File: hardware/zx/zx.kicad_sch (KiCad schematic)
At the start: 42 parts, among them J1 ZX Keyboard, J10 Conn_01x01, J11 Conn_01x01, J12 Conn_01x01, J13 Conn_01x01, J14 Conn_01x01, J15 Conn_01x01, J16 Conn_01x01, J17 Conn_01x01, J18 Conn_01x01, J19 Conn_01x01, J2 GOTEK, J20 Conn_01x01, J21 Conn_01x01, J22 Conn_01x01, J3 UART, J4 USB_A, J5 USB_A, J6 Keyboard, J7 Mouse, J8 Kempston Mouse, J9 Z80, SW1 RESET, SW2 BOOT0, SW3 BOOT1, U1 CH559L, U2 CH446Q, Y1 12MHz

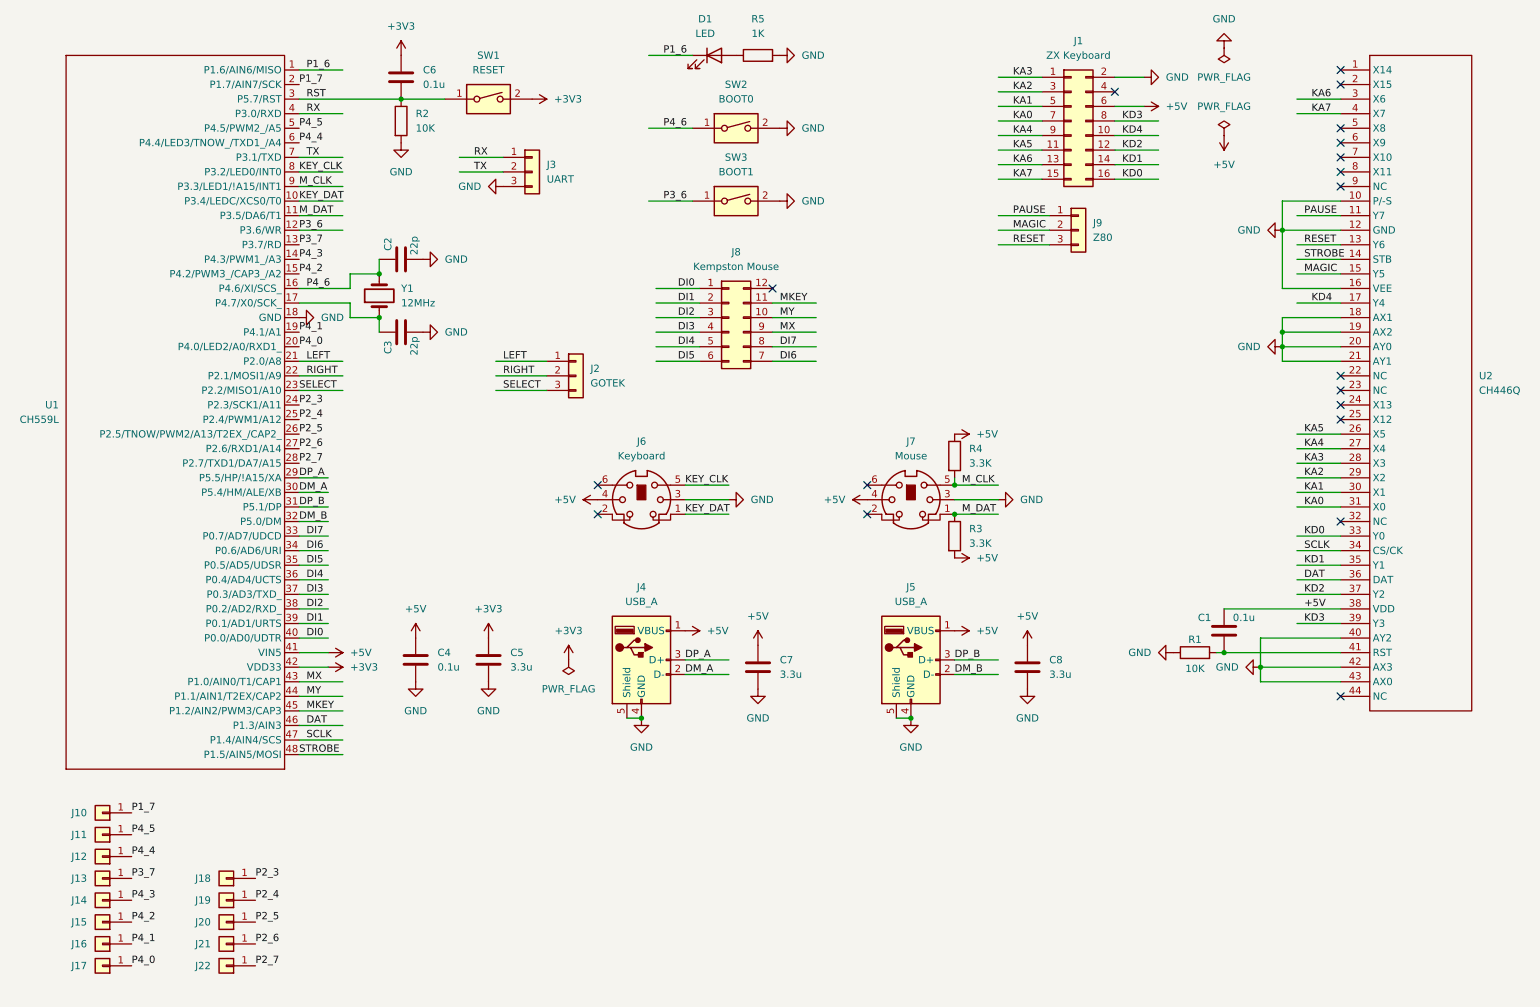
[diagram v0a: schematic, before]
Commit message: Initial PCB layout.
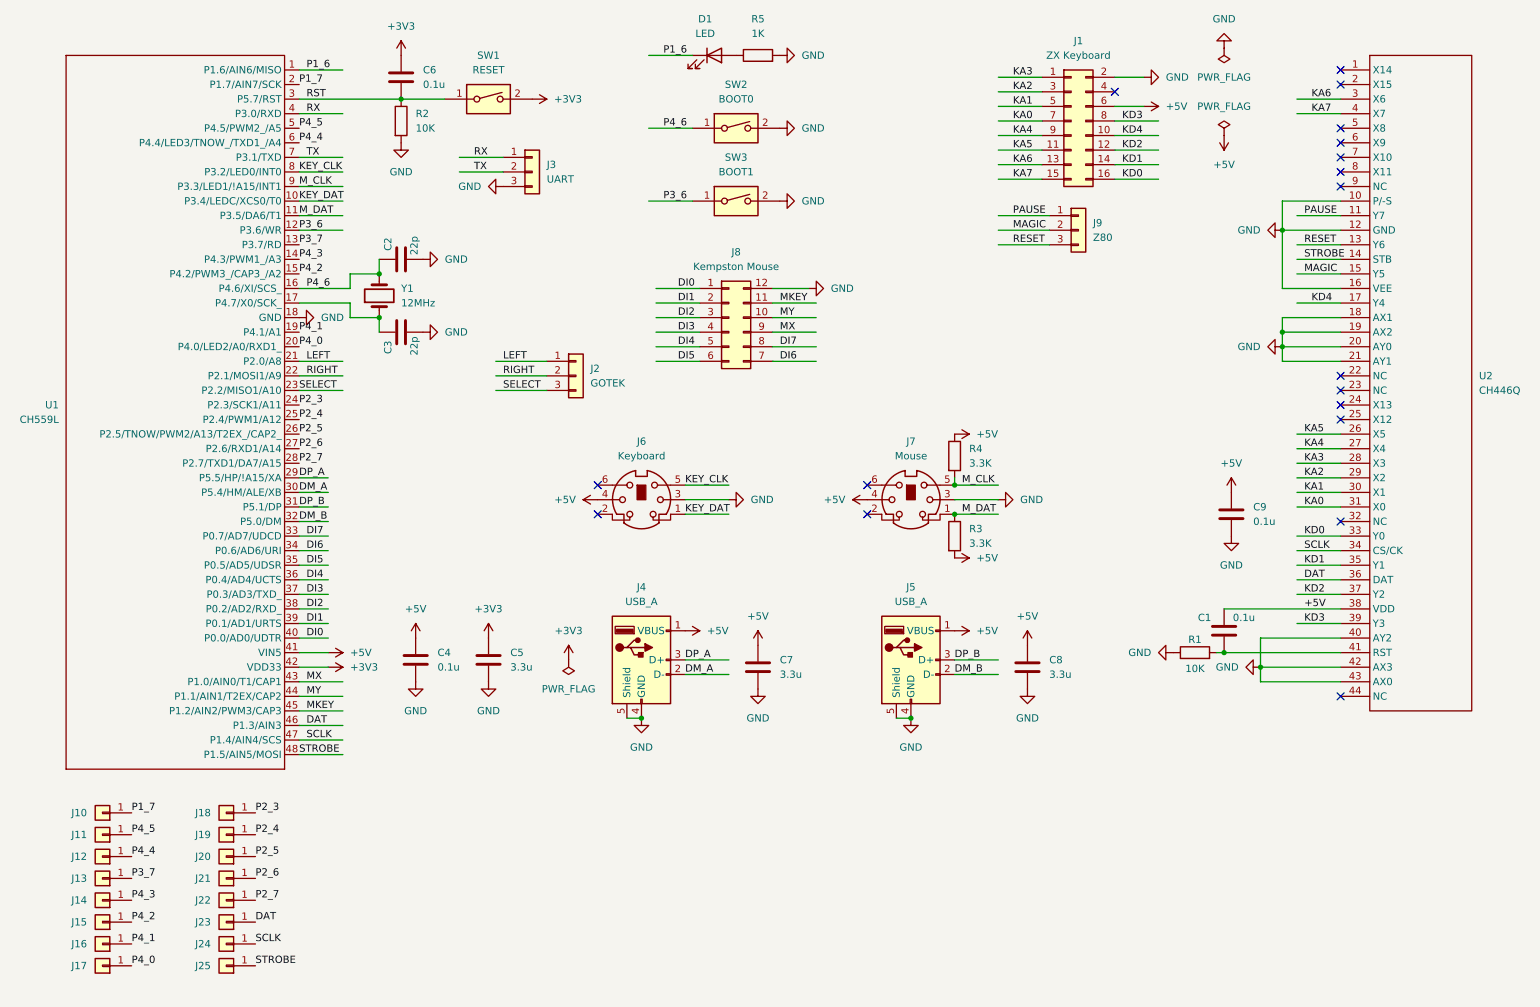
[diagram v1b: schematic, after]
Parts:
- added C9: 0.1u, Capacitor_SMD:C_1206_3216Metric_Pad1.33x1.80mm_HandSolder, symbol Device:C
- added J23, J24, J25: Conn_01x01, THT_Pin:THT_Pin_Vertical, symbol Connector_Generic:Conn_01x01
- J10, J11, J12, J13, J14, J15, J16, J17, J18, J19, J20, J21, J22: footprint Connector_PinHeader_2.54mm:PinHeader_1x01_P2.54mm_Vertical -> THT_Pin:THT_Pin_Vertical
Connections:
- net +5V: now also C9.1
- net DAT: now also J23.1 (Pin_1)
- net GND: now also J8.12 (Pin_12), C9.2
- net SCLK: now also J24.1 (Pin_1)
- net STROBE: now also J25.1 (Pin_1)
- no-connect marks 19 -> 18
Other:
- moved on the sheet: J18, J19, J20, J21, J22

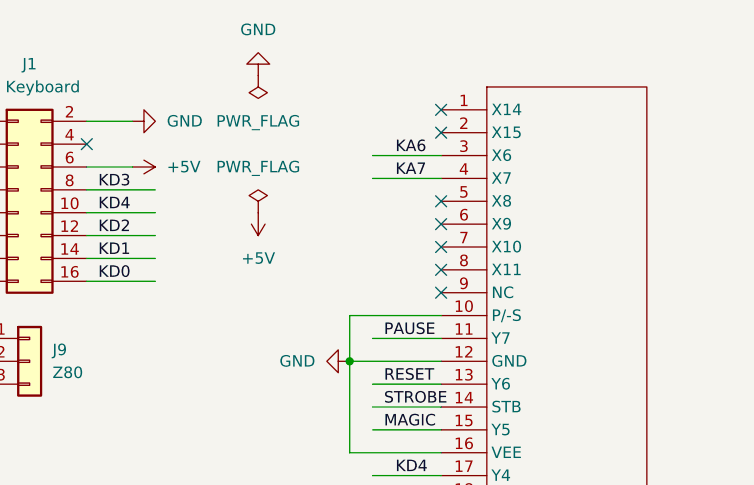
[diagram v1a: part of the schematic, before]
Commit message: CH446Q output Z80 control signals PAUSE, MAGIC, RESET have common input connected to GND.
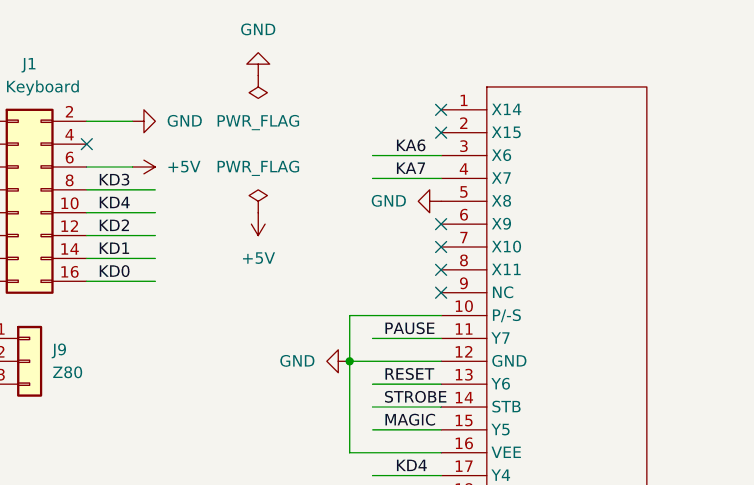
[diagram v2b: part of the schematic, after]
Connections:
- net GND: now also U2.5 (X8)
- no-connect marks 18 -> 17
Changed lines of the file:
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@@
 	)
 	(no_connect
-		(at 247.65 34.29)
-	)
-	(no_connect
 		(at 247.65 24.13)
 	)
@@
 					(unit 1)
 				)
+			)
+		)
+	)
+	(symbol
+		(lib_id "power:GND")
+		(at 247.65 34.29 270)
+		(unit 1)
+		(exclude_from_sim no)
+		(in_bom yes)
+		(on_board yes)
+		(dnp no)
+		(fields_autoplaced yes)
+		(property "Reference" "#PWR043"
+			(at 241.3 34.29 0)
+			(effects
+				(font
+					(size 1.27 1.27)
+				)
+				(hide yes)
+			)
+		)
+		(property "Value" "GND"
+			(at 243.84 34.2899 90)
+			(effects
+				(font
+					(size 1.27 1.27)
+				)
+				(justify right)
+			)
+		)
+		(property "Footprint" ""
+			(at 247.65 34.29 0)
+			(effects
+				(font
+					(size 1.27 1.27)
+				)
+				(hide yes)
+			)
+		)
+		(property "Datasheet" ""
+			(at 247.65 34.29 0)
+			(effects
+				(font
+					(size 1.27 1.27)
+				)
+				(hide yes)
+			)
+		)
+		(property "Description" "Power symbol creates a global label with name \"GND\" , ground"
+			(at 247.65 34.29 0)
+			(effects
+				(font
+					(size 1.27 1.27)
+				)
+				(hide yes)
+			)
+		)
+		(pin "1"
+		)
+		(instances
+			(project "zx"
+				(path "/e686a5db-35f9-40ca-bbb5-69eb58ec1522"
+					(reference "#PWR043")
+					(unit 1)
+				)

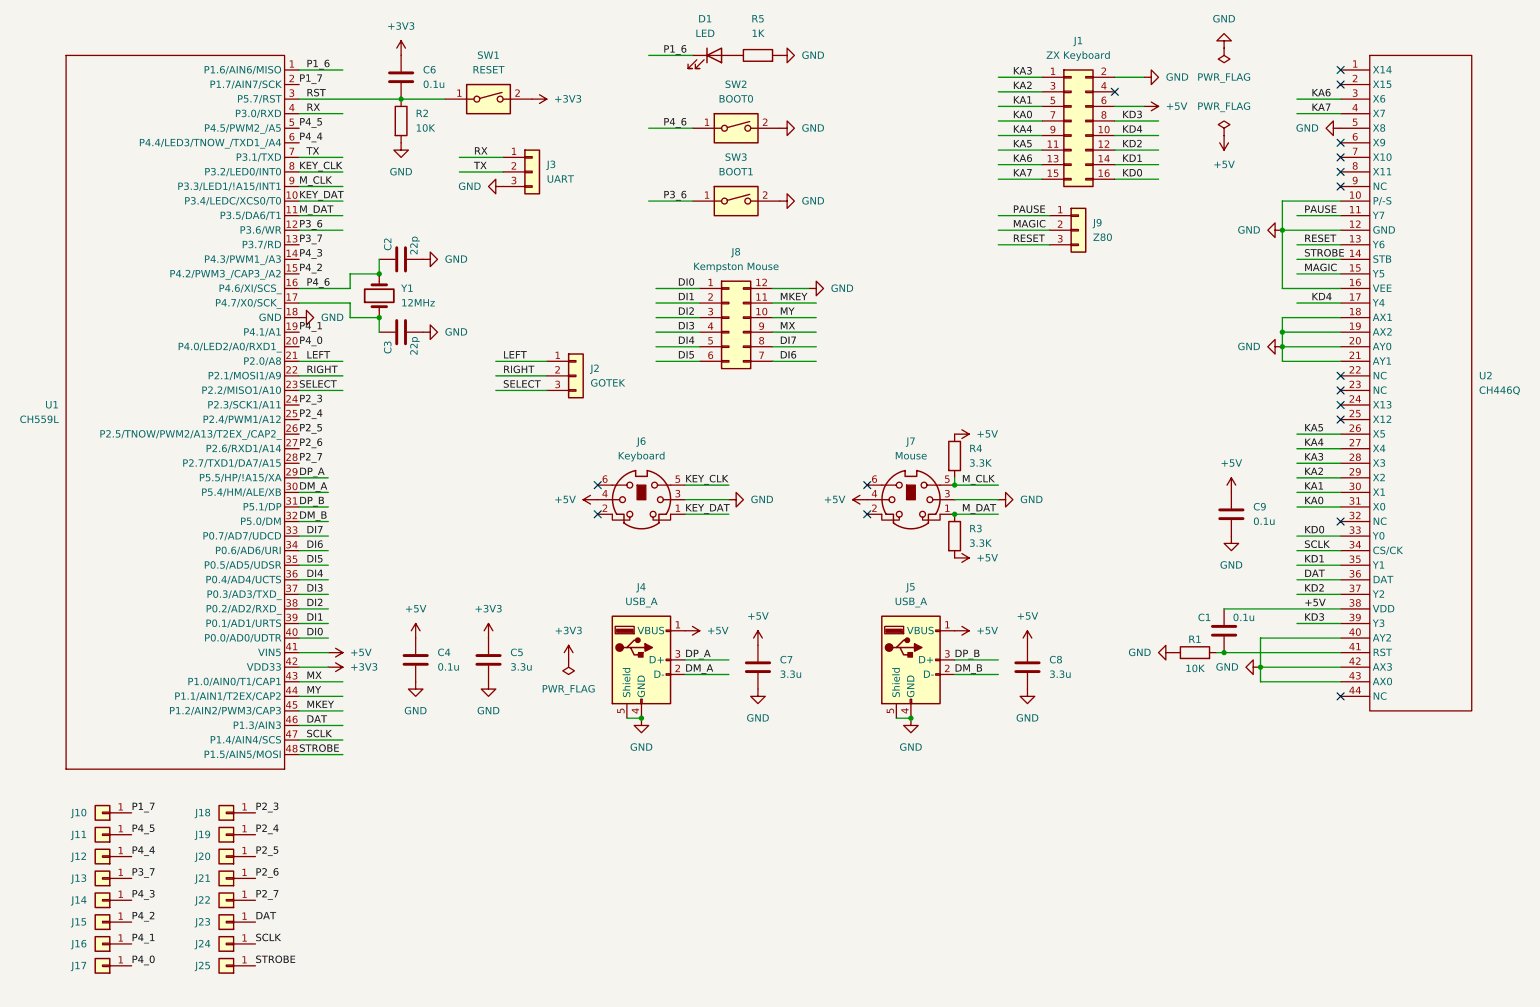
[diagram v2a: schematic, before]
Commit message: Reserve P1.6 for Kempston Joystick DI write strobe (JOY). Move activity LED to P1.7. Add free-standing GND pin. Add J8 GND label.
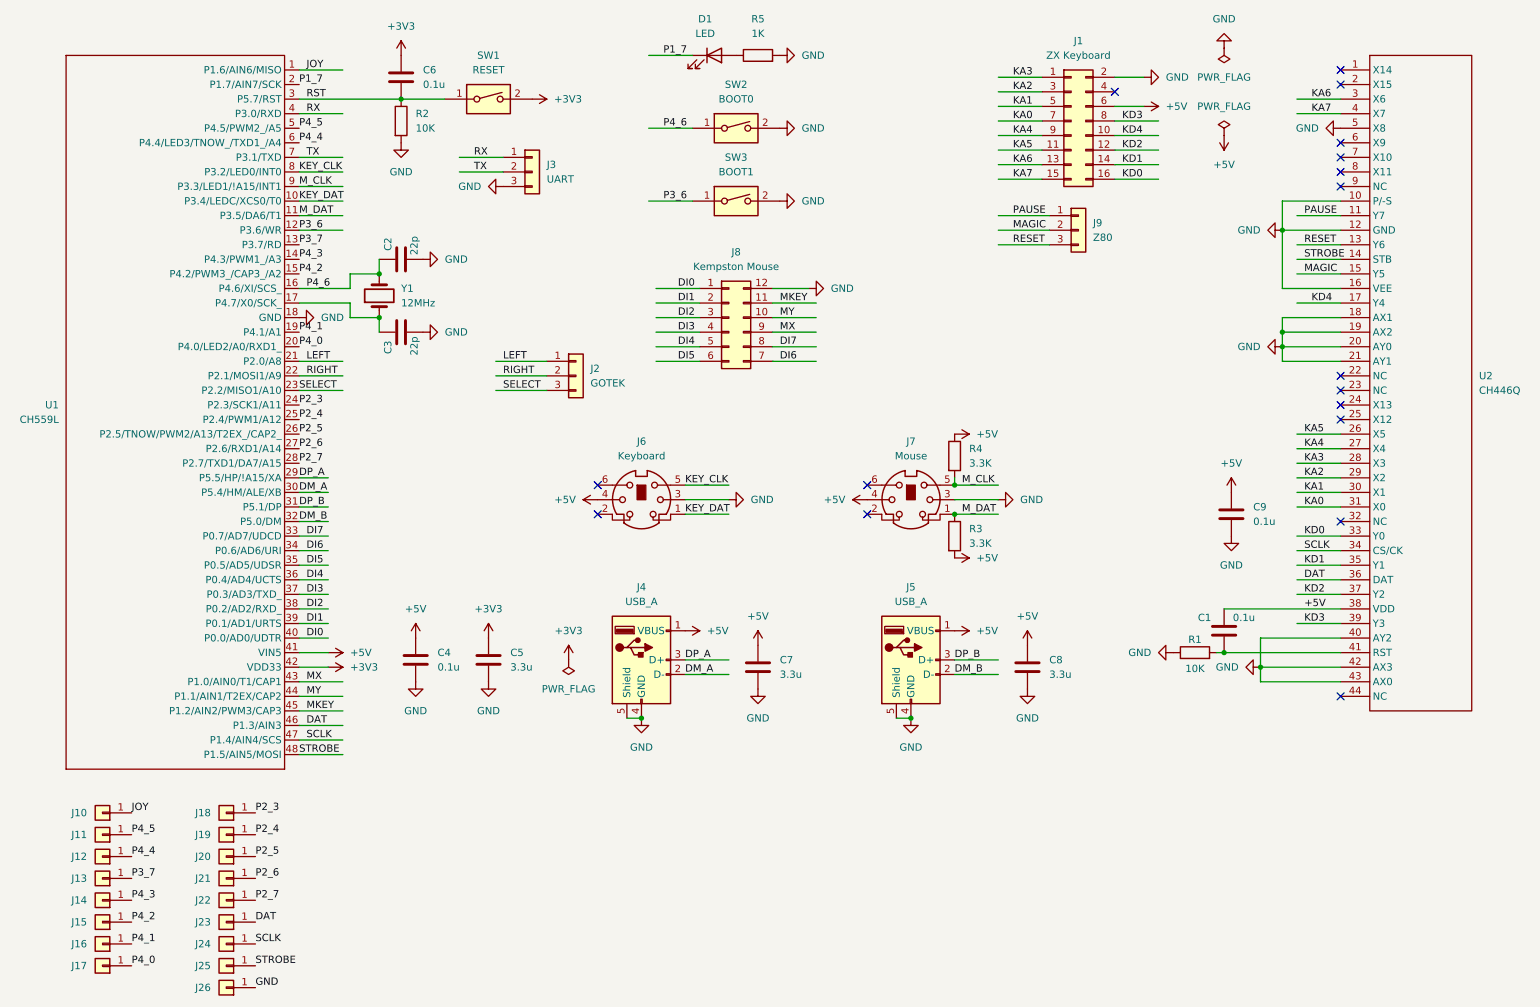
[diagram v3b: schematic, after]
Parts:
- added J26: Conn_01x01, THT_Pin:THT_Pin_Vertical, symbol Connector_Generic:Conn_01x01
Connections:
- net GND: now also J26.1 (Pin_1)
- net P1_7: now also D1.1 (K); no longer J10.1 (Pin_1)
- net P1_6 renamed JOY
- net JOY: now also J10.1 (Pin_1); no longer D1.1 (K)
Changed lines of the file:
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@@
 		)
 	)
-	(label "P1_6"
+	(label "P1_7"
 		(at 129.54 21.59 0)
 		(fields_autoplaced yes)
@@
 		)
 	)
-	(label "P1_7"
+	(label "JOY"
 		(at 36.83 153.67 0)
 		(fields_autoplaced yes)
@@
 		)
 	)
+	(label "GND"
+		(at 58.42 184.15 0)
+		(fields_autoplaced yes)
+		(effects
+			(font
+				(size 1.27 1.27)
+			)
+			(justify left bottom)
+		)
+	)
 	(label "PAUSE"
 		(at 241.3 49.53 0)
@@
 		)
 	)
-	(label "P1_6"
+	(label "JOY"
 		(at 67.31 24.13 0)
 		(fields_autoplaced yes)
@@
 					(unit 1)
 				)
+			)
+		)
+	)
+	(symbol
+		(lib_id "Connector_Generic:Conn_01x01")
+		(at 53.34 184.15 180)
+		(unit 1)
+		(exclude_from_sim no)
+		(in_bom yes)
+		(on_board yes)
+		(dnp no)
+		(property "Reference" "J26"
+			(at 49.276 184.15 0)
+			(effects
+				(font
+					(size 1.27 1.27)
+				)
+			)
+		)
+		(property "Value" "Conn_01x01"
+			(at 53.34 180.34 0)
+			(effects
+				(font
+					(size 1.27 1.27)
+				)
+				(hide yes)
+			)
+		)
+		(property "Footprint" "THT_Pin:THT_Pin_Vertical"
+			(at 53.34 184.15 0)
+			(effects
+				(font
+					(size 1.27 1.27)
+				)
+				(hide yes)
+			)
+		)
+		(property "Datasheet" "~"
+			(at 53.34 184.15 0)
+			(effects
+				(font
+					(size 1.27 1.27)
+				)
+				(hide yes)
+			)
+		)
+		(property "Description" "Generic connector, single row, 01x01, script generated (kicad-library-utils/schlib/autogen/connector/)"
+			(at 53.34 184.15 0)
+			(effects
+				(font
+					(size 1.27 1.27)
+				)
+				(hide yes)
+			)
+		)
+		(pin "1"
+		)
+		(instances
+			(project "zx"
+				(path "/e686a5db-35f9-40ca-bbb5-69eb58ec1522"
+					(reference "J26")
+					(unit 1)
+				)

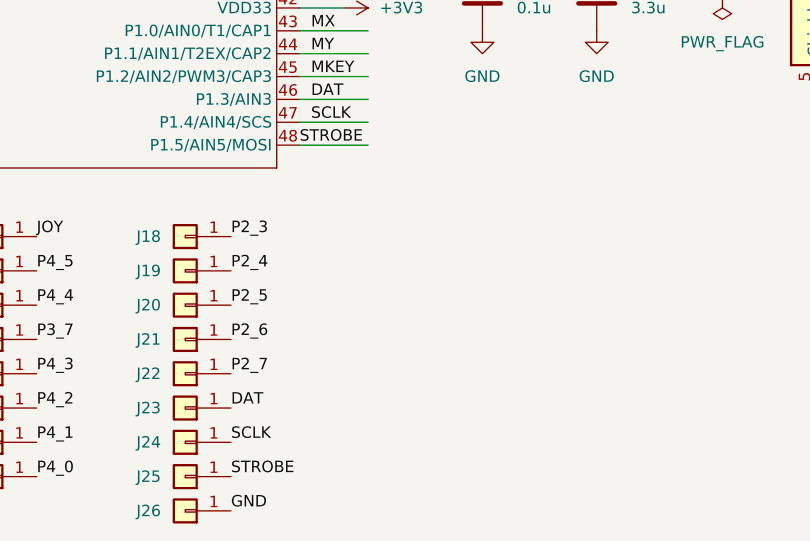
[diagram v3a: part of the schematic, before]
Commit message: Add PS/2 keyboard/mouse debug pins.
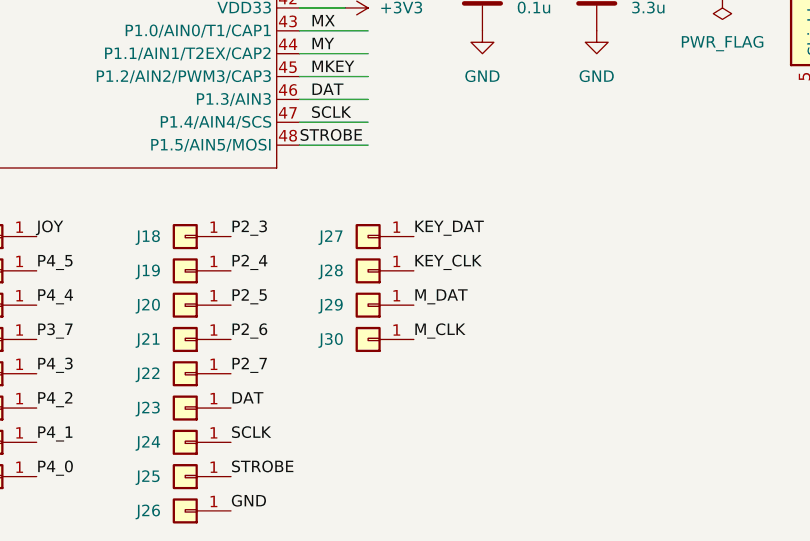
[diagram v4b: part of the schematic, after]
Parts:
- added J27, J28, J29, J30: Conn_01x01, THT_Pin:THT_Pin_Vertical, symbol Connector_Generic:Conn_01x01
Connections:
- net KEY_CLK: now also J28.1 (Pin_1)
- net KEY_DAT: now also J27.1 (Pin_1)
- net M_CLK: now also J30.1 (Pin_1)
- net M_DAT: now also J29.1 (Pin_1)
